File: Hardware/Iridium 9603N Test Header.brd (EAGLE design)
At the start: 29.6 x 31.5 mm, 3 parts, among them J3 SS4-10-3.50-X-D

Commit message: Added the dimensions
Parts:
- moved J2 22.9 mm to (2.10, 29.2), turned to 270 degrees
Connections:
- net N$11: now also J2.10; no longer J2.1
- net N$12: now also J2.9; no longer J2.2
- net N$13: now also J2.8; no longer J2.3
- net N$14: now also J2.7; no longer J2.4
- net N$15: now also J2.6; no longer J2.5
- net N$16: now also J2.5; no longer J2.6
- net N$17: now also J2.4; no longer J2.7
- net N$18: now also J2.3; no longer J2.8
- net N$19: now also J2.2; no longer J2.9
- net N$20: now also J2.1; no longer J2.10
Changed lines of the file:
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@@
 <dimension x1="0" y1="31.5" x2="0" y2="0" x3="-5" y3="15.75" textsize="1.778" layer="51" dtype="vertical"/>
 <dimension x1="0" y1="31.5" x2="29.6" y2="31.5" x3="14.8" y3="36.5" textsize="1.778" layer="51" dtype="horizontal"/>
+<dimension x1="2.3" y1="2.5" x2="27.3" y2="2.5" x3="14.8" y3="-5" textsize="1.778" layer="51" dtype="horizontal"/>
+<dimension x1="0" y1="0" x2="2.3" y2="2.5" x3="-2" y3="1.25" textsize="1.778" layer="51" dtype="vertical"/>
+<dimension x1="27.3" y1="2.5" x2="29.6" y2="0" x3="28.45" y3="-5" textsize="1.778" layer="51" dtype="horizontal"/>
 </plain>
 <attributes>
@@
 <attribute name="VALUE" x="25.468" y="30.48" size="0.6096" layer="27" font="vector" ratio="20" rot="R270"/>
 </element>
-<element name="J2" library="SparkFun-Connectors" library_urn="urn:adsk.eagle:library:513" package="1X10" package3d_urn="urn:adsk.eagle:package:38157/1" value="" x="2.1" y="6.35" smashed="yes" rot="R90">
-<attribute name="PROD_ID" value="CONN-11563" x="2.1" y="6.35" size="1.778" layer="27" rot="R90" display="off"/>
-<attribute name="VALUE" x="4.132" y="5.08" size="0.6096" layer="27" font="vector" ratio="20" rot="R90"/>
+<element name="J3" library="Iridium 9603N Test Header" package="SS4-10-3.50-X-D" value="SS4-10-3.50-X-D" x="12.3" y="28.1" smashed="yes" rot="MR180"/>
+<element name="J2" library="SparkFun-Connectors" library_urn="urn:adsk.eagle:library:513" package="1X10" package3d_urn="urn:adsk.eagle:package:38157/1" value="" x="2.1" y="29.21" smashed="yes" rot="R270">
+<attribute name="PROD_ID" value="CONN-11563" x="2.1" y="29.21" size="1.778" layer="27" rot="R270" display="off"/>
+<attribute name="VALUE" x="0.068" y="30.48" size="0.6096" layer="27" font="vector" ratio="20" rot="R270"/>
 </element>
-<element name="J3" library="Iridium 9603N Test Header" package="SS4-10-3.50-X-D" value="SS4-10-3.50-X-D" x="12.3" y="28.1" smashed="yes" rot="MR180"/>
 </elements>
 <signals>
@@
 <signal name="N$11">
 <contactref element="J3" pad="20"/>
-<contactref element="J2" pad="1"/>
 <wire x1="10.5" y1="30.435" x2="9.835" y2="30.435" width="0.2032" layer="16"/>
 <wire x1="9.835" y1="30.435" x2="9.8" y2="30.4" width="0.2032" layer="16"/>
@@
 <wire x1="3.8" y1="8.05" x2="2.1" y2="6.35" width="0.3048" layer="16"/>
 <wire x1="3.8" y1="27.9" x2="3.8" y2="8.05" width="0.3048" layer="16"/>
+<contactref element="J2" pad="10"/>
 </signal>
 <signal name="N$12">
 <contactref element="J3" pad="18"/>
-<contactref element="J2" pad="2"/>
 <wire x1="10.9" y1="30.435" x2="10.9" y2="29.8" width="0.2032" layer="16"/>
 <wire x1="10.9" y1="29.8" x2="10.8" y2="29.7" width="0.2032" layer="16"/>
@@
 <wire x1="2.11" y1="8.9" x2="2.1" y2="8.89" width="0.508" layer="1"/>
 <wire x1="4.433" y1="27.733" x2="4.433" y2="8.921" width="0.3048" layer="16"/>
+<contactref element="J2" pad="9"/>
 </signal>
 <signal name="N$13">
 <contactref element="J3" pad="16"/>
-<contactref element="J2" pad="3"/>
 <wire x1="2.1" y1="11.43" x2="5.07" y2="11.43" width="0.508" layer="1"/>
 <wire x1="5.07" y1="11.43" x2="5.1" y2="11.4" width="0.508" layer="1"/>
@@
 <wire x1="11.3" y1="29.73585" x2="11.3" y2="30.435" width="0.2032" layer="16"/>
 <wire x1="9.6" y1="29.367" x2="6.967" y2="29.367" width="0.3048" layer="16"/>
+<contactref element="J2" pad="8"/>
 </signal>
 <signal name="N$14">
 <contactref element="J3" pad="14"/>
-<contactref element="J2" pad="4"/>
 <wire x1="10.8671" y1="28.8388" x2="10.8" y2="28.8388" width="0.2032" layer="16"/>
 <wire x1="10.8" y1="28.8388" x2="7.2388" y2="28.8388" width="0.3048" layer="16"/>
@@
 <wire x1="11.7" y1="30.435" x2="11.7" y2="29.6717" width="0.2032" layer="16"/>
 <wire x1="11.7" y1="29.6717" x2="10.8671" y2="28.8388" width="0.2032" layer="16"/>
+<contactref element="J2" pad="7"/>
 </signal>
 <signal name="N$15">
 <contactref element="J3" pad="12"/>
-<contactref element="J2" pad="5"/>
 <wire x1="12.1" y1="30.435" x2="12.1" y2="29.6" width="0.2032" layer="16"/>
 <wire x1="10.8" y1="28.3" x2="10.7" y2="28.3" width="0.2032" layer="16"/>
@@
 <wire x1="7.5" y1="28.3" x2="6.3" y2="27.1" width="0.3048" layer="16"/>
 <wire x1="6.3" y1="27.1" x2="6.3" y2="16.5" width="0.3048" layer="16"/>
+<contactref element="J2" pad="6"/>
 </signal>
 <signal name="N$16">
 <contactref element="J3" pad="10"/>
-<contactref element="J2" pad="6"/>
 <wire x1="12.5" y1="30.435" x2="12.5" y2="29.4" width="0.2032" layer="16"/>
 <wire x1="10.9" y1="27.8" x2="10.8" y2="27.8" width="0.2032" layer="16"/>
@@
 <wire x1="7.9" y1="27.8" x2="6.9" y2="26.8" width="0.3048" layer="16"/>
 <wire x1="6.9" y1="26.8" x2="6.9" y2="19" width="0.3048" layer="16"/>
+<contactref element="J2" pad="5"/>
 </signal>
 <signal name="N$17">
 <contactref element="J3" pad="8"/>
-<contactref element="J2" pad="7"/>
 <wire x1="12.9" y1="30.435" x2="12.9" y2="29.1" width="0.2032" layer="16"/>
 <wire x1="11.1" y1="27.3" x2="11" y2="27.3" width="0.2032" layer="16"/>
@@
 <wire x1="8.3" y1="27.3" x2="7.5" y2="26.5" width="0.3048" layer="16"/>
 <wire x1="7.5" y1="26.5" x2="7.5" y2="21.6" width="0.3048" layer="16"/>
+<contactref element="J2" pad="4"/>
 </signal>
 <signal name="N$18">
 <contactref element="J3" pad="6"/>
-<contactref element="J2" pad="8"/>
 <wire x1="13.3" y1="30.435" x2="13.3" y2="28.9" width="0.2032" layer="16"/>
 <wire x1="11.1" y1="26.7" x2="11" y2="26.7" width="0.2032" layer="16"/>
@@
 <wire x1="2.13" y1="24.1" x2="2.1" y2="24.13" width="0.3048" layer="1"/>
 <wire x1="13.3" y1="28.9" x2="11.1" y2="26.7" width="0.2032" layer="16"/>
+<contactref element="J2" pad="3"/>
 </signal>
 <signal name="N$19">
 <contactref element="J3" pad="4"/>
-<contactref element="J2" pad="9"/>
 <wire x1="13.7" y1="30.435" x2="13.7" y2="29.4" width="0.2032" layer="16"/>
 <wire x1="13.7" y1="29.4" x2="14" y2="29.1" width="0.2032" layer="16"/>
@@
 <wire x1="12.8" y1="27.4" x2="2.83" y2="27.4" width="0.508" layer="1"/>
 <wire x1="2.83" y1="27.4" x2="2.1" y2="26.67" width="0.508" layer="1"/>
+<contactref element="J2" pad="2"/>
 </signal>
 <signal name="N$20">
 <contactref element="J3" pad="2"/>
-<contactref element="J2" pad="10"/>
 <wire x1="14.1" y1="30.435" x2="14.765" y2="30.435" width="0.2032" layer="16"/>
 <wire x1="14.765" y1="30.435" x2="14.8" y2="30.4" width="0.2032" layer="16"/>
@@
 <wire x1="14.8" y1="28.5" x2="2.81" y2="28.5" width="0.508" layer="1"/>
 <wire x1="2.81" y1="28.5" x2="2.1" y2="29.21" width="0.508" layer="1"/>
+<contactref element="J2" pad="1"/>
 </signal>
 </signals>

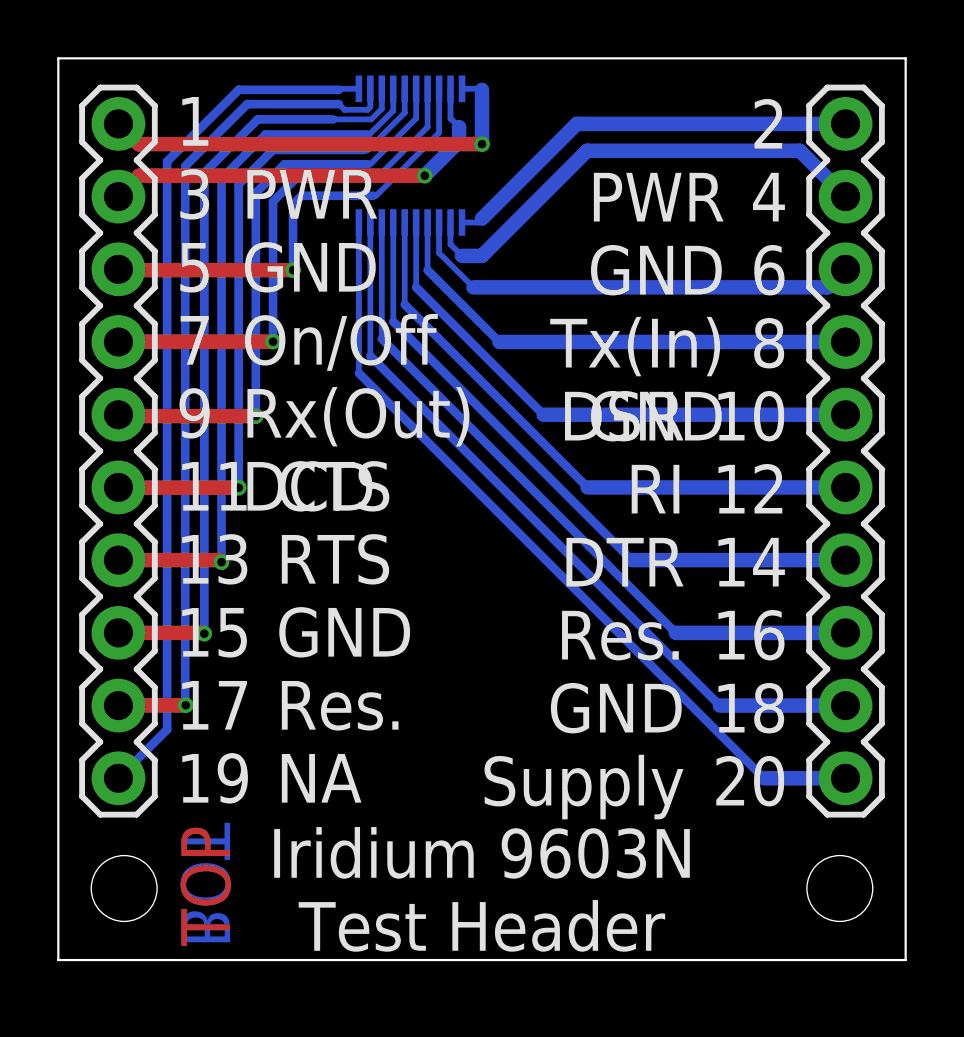
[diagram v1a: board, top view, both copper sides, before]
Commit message: Corrected the ST4-10-2.50 footprint
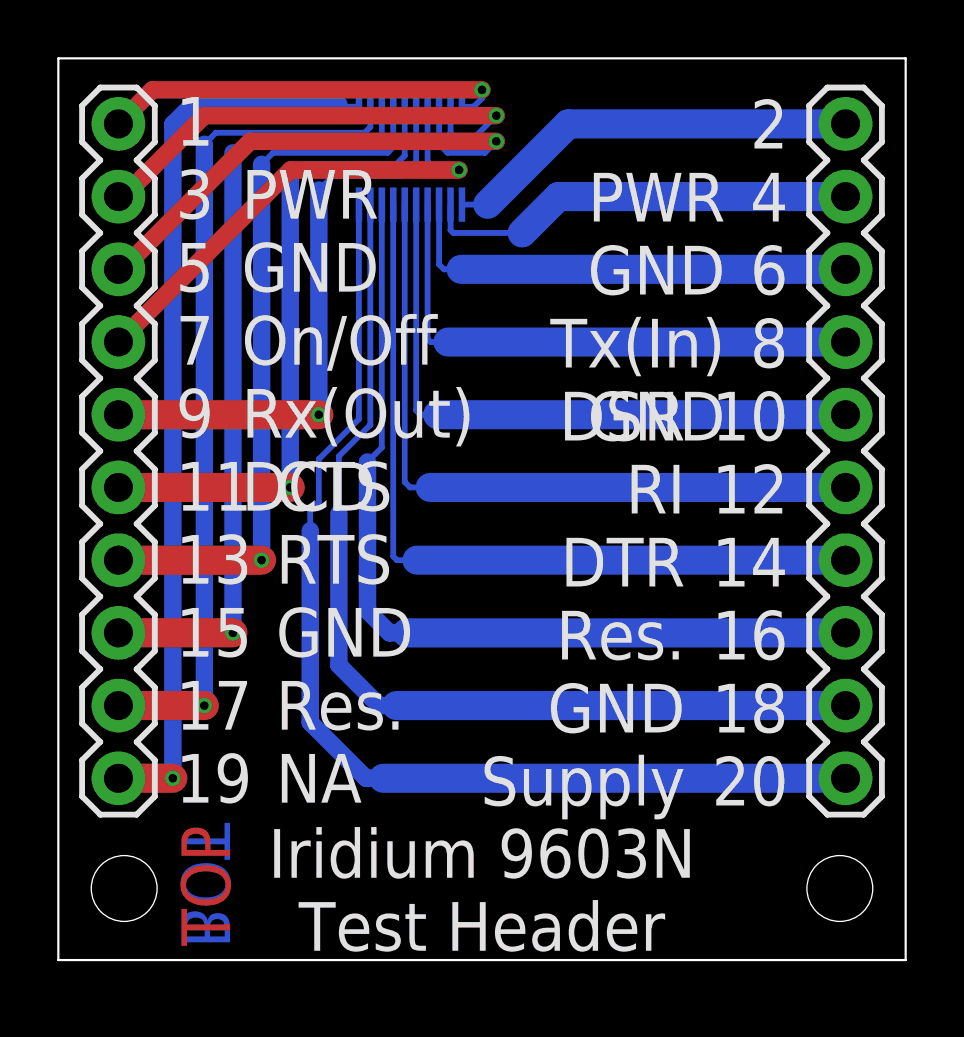
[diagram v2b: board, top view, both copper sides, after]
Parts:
- J3: value SS4-10-3.50-X-D -> ST4-10-X.XX-X-D; device Iridium 9603N Test Header:SS4-10-3.50-X-D -> ST4-30-X.XX-X-D:ST4-10-X.XX-X-D
- moved J1 25.4 mm to (2.10, 29.2)
- moved J2 25.4 mm to (27.5, 29.2)
- turned J3 to 0 degrees
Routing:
- net N$20: track 30.0 -> 38.3 mm
- net N$18: track 29.3 -> 34.8 mm, vias 1 -> 0
- net N$16: track 26.9 -> 31.4 mm, vias 1 -> 0
- net N$19: track 28.1 -> 31.6 mm, vias 0 -> 1
- net N$14: track 24.8 -> 28.1 mm, vias 1 -> 0
- net N$17: track 26.3 -> 29.4 mm, vias 0 -> 1
- net N$15: track 24.5 -> 27.2 mm, vias 0 -> 1
- net N$12: track 22.5 -> 25.2 mm, vias 1 -> 0
- net N$5: track 16.0 -> 18.7 mm, vias 0 -> 1
- net N$13: track 22.7 -> 25.1 mm, vias 0 -> 1
- net N$11: track 20.9 -> 22.8 mm, vias 0 -> 1
- net N$10: track 20.3 -> 22.3 mm, vias 1 -> 0
- net N$9: track 19.1 -> 20.6 mm, vias 0 -> 1
- net N$8: track 18.1 -> 19.3 mm, vias 1 -> 0
- net N$2: track 15.6 -> 14.7 mm, vias 1 -> 0
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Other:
- board text removed: "ST4-10-2.50"
